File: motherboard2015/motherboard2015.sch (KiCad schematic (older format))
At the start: 29 parts, among them J1 RJ45, J2 RJ45, J3 RJ45, J4 RJ45, P1 DIL40

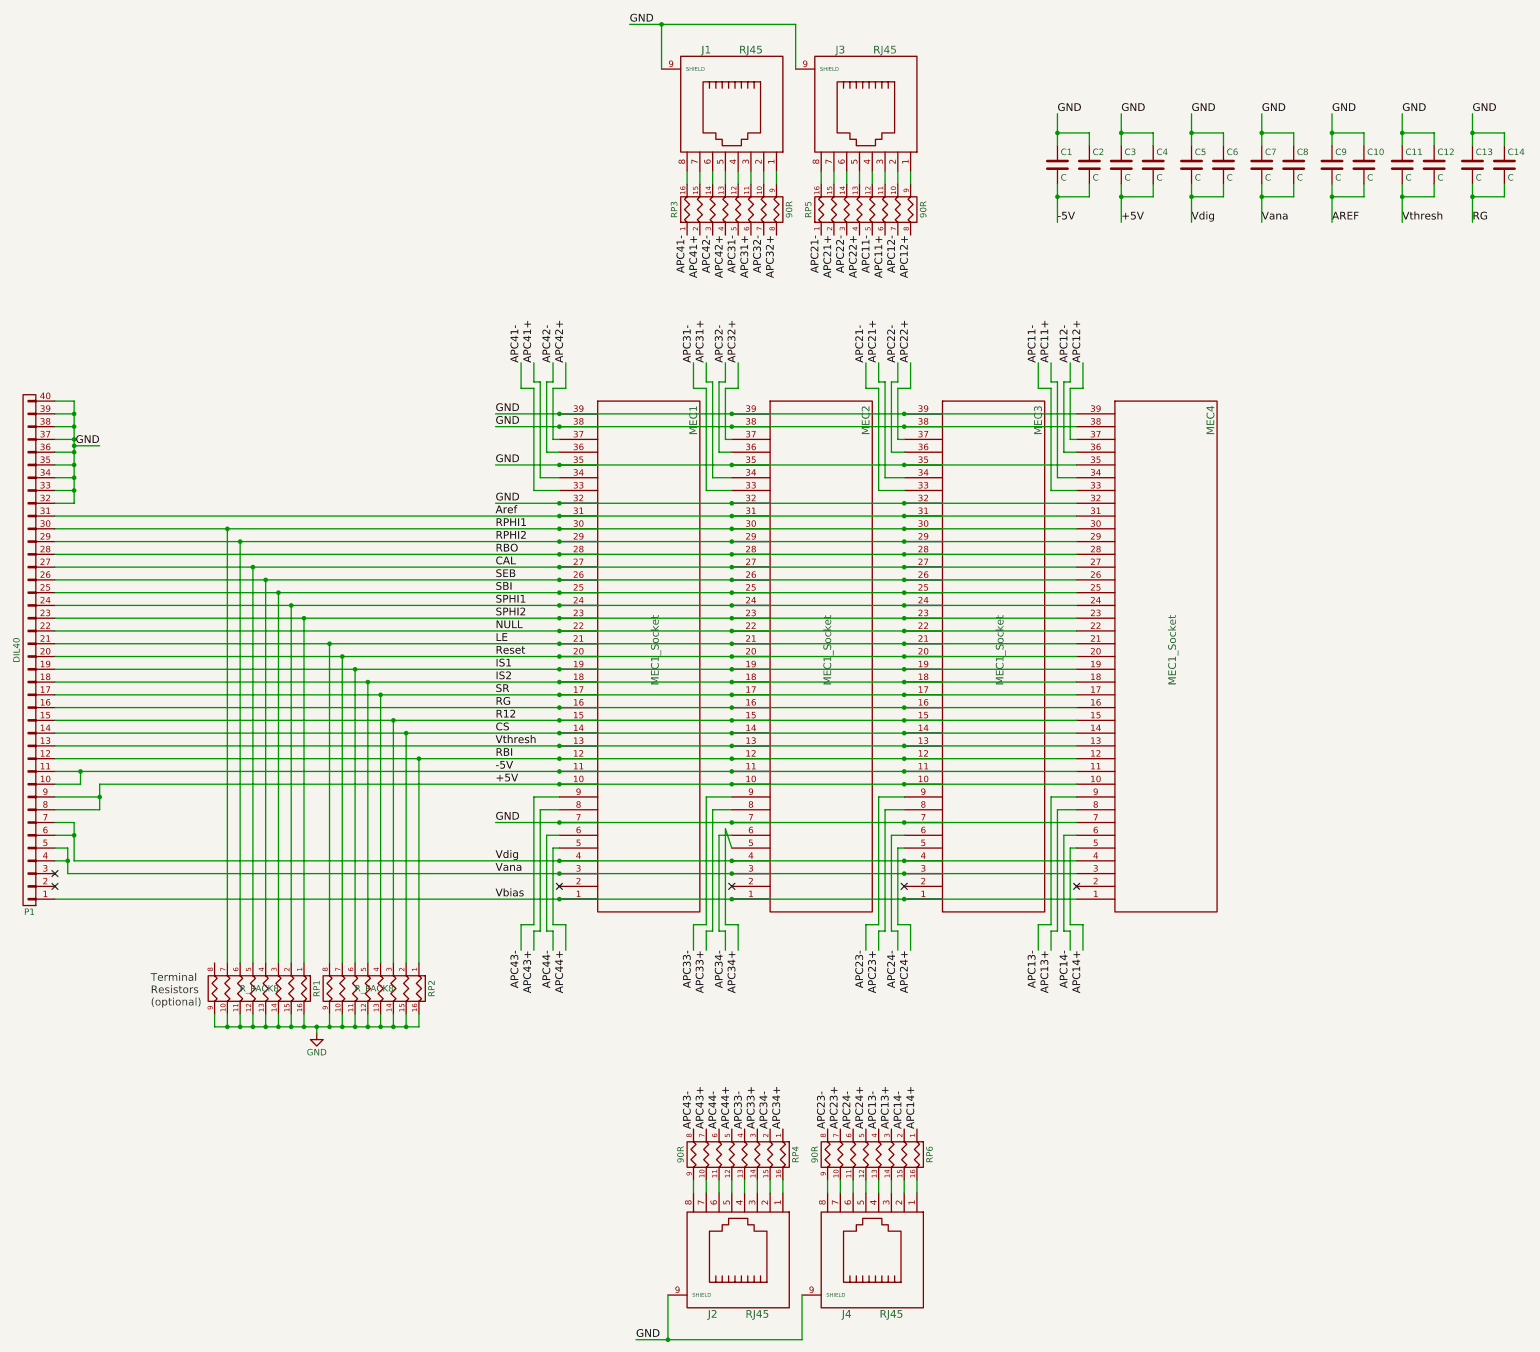
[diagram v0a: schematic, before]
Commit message: Updates to DAQ system including adjusting position of ZEM and adding Control signal outputs
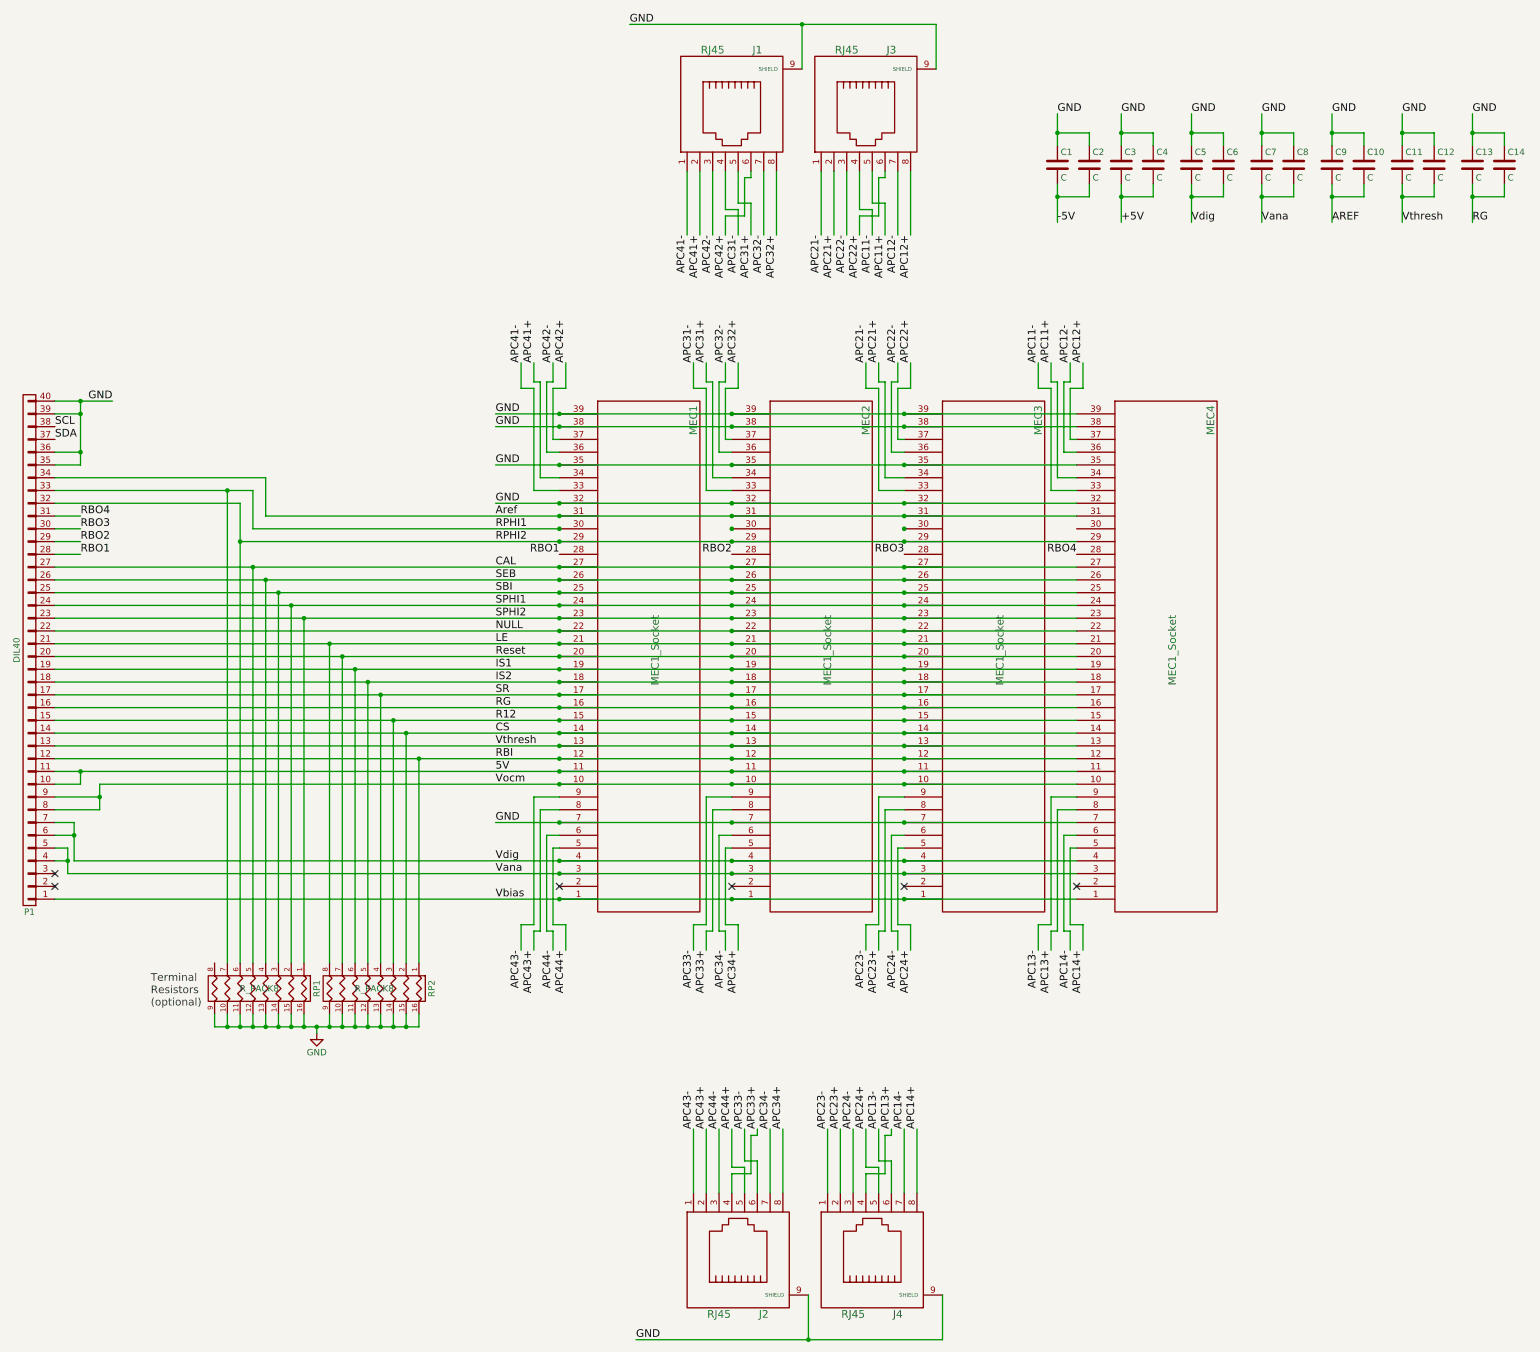
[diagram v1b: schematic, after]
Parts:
- removed RP3, RP4, RP5, RP6: 90R, extras:R8_MNR18, symbol R_PACK8
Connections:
- net +5V: no longer MEC1.10 (P10), MEC2.10 (P10), MEC3.10 (P10), MEC4.10 (P10), P1.8 (P8), P1.9 (P9)
- net -5V: no longer MEC1.11 (P11), MEC2.11 (P11), MEC3.11 (P11), MEC4.11 (P11), P1.10 (P10), P1.11 (P11)
- net APC11+: now also J3.5
- net APC11-: now also J3.4
- net APC12+: now also J3.8
- net APC12-: now also J3.7
- net APC13+: now also J4.4
- net APC13-: now also J4.6
- net APC14+: now also J4.8
- net APC14-: now also J4.7
- net APC21+: now also J3.2
- net APC21-: now also J3.1
- net APC22+: now also J3.6
- net APC22-: now also J3.3
- net APC23+: now also J4.2
- net APC23-: now also J4.1
- net APC24+: now also J4.5
- net APC24-: now also J4.3
- net APC31+: now also J1.5
- net APC31-: now also J1.4
- net APC32+: now also J1.8
- net APC32-: now also J1.7
- net APC33+: now also J2.4
- net APC33-: now also J2.6
- net APC34+: now also J2.8
- net APC34-: now also J2.7
- net APC41+: now also J1.2
- net APC41-: now also J1.1
- net APC42+: now also J1.6
- net APC42-: now also J1.3
- net APC43+: now also J2.2
- net APC43-: now also J2.1
- net APC44+: now also J2.5
- net APC44-: now also J2.3
- net Aref: now also P1.34 (P34); no longer P1.31 (P31)
- net GND: no longer P1.32 (P32), P1.33 (P33), P1.34 (P34), P1.37 (P37), P1.38 (P38)
- net RPHI1: now also P1.33 (P33); no longer MEC2.30 (P30), MEC3.30 (P30), MEC4.30 (P30), P1.30 (P30)
- net RPHI2: now also P1.32 (P32); no longer P1.29 (P29)
- removed net RBO: MEC1.28 (P28), MEC2.28 (P28), MEC3.28 (P28), MEC4.28 (P28), P1.28 (P28)
- new net 5V: MEC1.11 (P11), MEC2.11 (P11), MEC3.11 (P11), MEC4.11 (P11), P1.10 (P10), P1.11 (P11)
- new net RBO1: MEC1.28 (P28), P1.28 (P28)
- new net RBO2: MEC2.28 (P28), P1.29 (P29)
- new net RBO3: MEC3.28 (P28), P1.30 (P30)
- new net RBO4: MEC4.28 (P28), P1.31 (P31)
- new net SCL: P1.38 (P38)
- new net SDA: P1.37 (P37)
- new net Vocm: MEC1.10 (P10), MEC2.10 (P10), MEC3.10 (P10), MEC4.10 (P10), P1.8 (P8), P1.9 (P9)
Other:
- moved on the sheet: J1, J2, J3, J4

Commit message: bunch of updates
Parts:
- MEC1, MEC2, MEC3, MEC4: digipart (none) -> SAM8119-ND
- P1: footprint Pin_Headers:Pin_Header_Straight_2x20 -> extras:Pin_Header_Straight_2x20
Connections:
- net APC33+: now also J2.5; no longer J2.4
- net APC33-: now also J2.3; no longer J2.6
- net APC34+: now also J2.2; no longer J2.8
- net APC34-: now also J2.1; no longer J2.7
- net APC43+: now also J2.8; no longer J2.2
- net APC43-: now also J2.7; no longer J2.1
- net APC44+: now also J2.4; no longer J2.5
- net APC44-: now also J2.6; no longer J2.3

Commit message: Additional work on motherboard, removes some extraneous files
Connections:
- net APC13+: now also J4.5; no longer J4.4
- net APC13-: now also J4.3; no longer J4.6
- net APC14+: now also J4.2; no longer J4.8
- net APC14-: now also J4.1; no longer J4.7
- net APC23+: now also J4.8; no longer J4.2
- net APC23-: now also J4.7; no longer J4.1
- net APC24+: now also J4.4; no longer J4.5
- net APC24-: now also J4.6; no longer J4.3
- net CAL: now also RP1.12 (R5); no longer RP1.5 (P5)
- net CS: now also RP2.15 (R2); no longer RP2.2 (P2)
- net GND: now also RP1.1 (P1), RP1.2 (P2), RP1.3 (P3), RP1.4 (P4), RP1.5 (P5), RP1.6 (P6), RP1.7 (P7), RP1.8 (P8), RP2.1 (P1), RP2.2 (P2), RP2.3 (P3), RP2.4 (P4), RP2.5 (P5), RP2.6 (P6), RP2.7 (P7), RP2.8 (P8); no longer RP1.10 (R7), RP1.11 (R6), RP1.12 (R5), RP1.13 (R4), RP1.14 (R3), RP1.15 (R2), RP1.16 (R1), RP1.9 (R8), RP2.10 (R7), RP2.11 (R6), RP2.12 (R5), RP2.13 (R4), RP2.14 (R3), RP2.15 (R2), RP2.16 (R1), RP2.9 (R8)
- net IS1: now also RP2.11 (R6); no longer RP2.6 (P6)
- net IS2: now also RP2.12 (R5); no longer RP2.5 (P5)
- net LE: now also RP2.9 (R8); no longer RP2.8 (P8)
- net R12: now also RP2.14 (R3); no longer RP2.3 (P3)
- net RBI: now also RP2.16 (R1); no longer RP2.1 (P1)
- net RPHI1: now also RP1.10 (R7); no longer RP1.7 (P7)
- net RPHI2: now also RP1.11 (R6); no longer RP1.6 (P6)
- net Reset: now also RP2.10 (R7); no longer RP2.7 (P7)
- net SBI: now also RP1.14 (R3); no longer RP1.3 (P3)
- net SEB: now also RP1.13 (R4); no longer RP1.4 (P4)
- net SPHI1: now also RP1.15 (R2); no longer RP1.2 (P2)
- net SPHI2: now also RP1.16 (R1); no longer RP1.1 (P1)
- net SR: now also RP2.13 (R4); no longer RP2.4 (P4)
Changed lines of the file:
@@
 Text Label 7400 11000 0    60   ~ 0
 GND
+Text Label 9000 9350 1    60   ~ 0
+APC14+
+Text Label 8900 9350 1    60   ~ 0
+APC14-
+Text Label 9200 9350 1    60   ~ 0
+APC13+
+Text Label 9100 9350 1    60   ~ 0
+APC13-
+Text Label 9400 9350 1    60   ~ 0
+APC24+
+Text Label 9300 9350 1    60   ~ 0
+APC24-
 Text Label 9600 9350 1    60   ~ 0
-APC14+
+APC23+
 Text Label 9500 9350 1    60   ~ 0
-APC14-
-Text Label 9400 9350 1    60   ~ 0
-APC13+
-Text Label 9300 9350 1    60   ~ 0
-APC13-
-Text Label 9200 9350 1    60   ~ 0
-APC24+
-Text Label 9100 9350 1    60   ~ 0
-APC24-
-Text Label 9000 9350 1    60   ~ 0
-APC23+
-Text Label 8900 9350 1    60   ~ 0
 APC23-
 Text Label 7950 9350 1    60   ~ 0
@@
 F 3 "" H 5350 8250 60  0000 C CNN
 	1    5350 8250
-	0    1    1    0
+	0    1    -1   0
 $EndComp
 $Comp
@@
 F 3 "" H 4450 8250 60  0000 C CNN
 	1    4450 8250
-	0    1    1    0
+	0    1    -1   0
 $EndComp
 $Comp
@@
 	6800 4650 4400 4650
 Wire Wire Line
-	4400 4350 4400 4650
-Wire Wire Line
-	2850 4350 4400 4350
+	4400 4650 4400 4350
+Wire Wire Line
+	4400 4350 2850 4350
 Wire Wire Line
 	4300 4450 2850 4450

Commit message: annotates parts for new build-management tool
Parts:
- C1, C10, C11, C12, C13, C14, C2, C3, C4, C5, C6, C7, C8, C9: footprint SMD_Packages:SMD-0603 -> Capacitors_SMD:C_0603
- MEC1, MEC2, MEC3, MEC4: Digikey (none) -> SAM8119-ND; digipart SAM8119-ND -> (none)
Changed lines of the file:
@@
 F 0 "C9" H 12875 1900 50  0000 L CNN
 F 1 "C" H 12875 1700 50  0000 L CNN
-F 2 "SMD_Packages:SMD-0603" H 12888 1650 30  0001 C CNN
+F 2 "Capacitors_SMD:C_0603" H 12888 1650 30  0001 C CNN
 F 3 "" H 12850 1800 60  0000 C CNN
 	1    12850 1800
@@
 F 0 "C11" H 13425 1900 50  0000 L CNN
 F 1 "C" H 13425 1700 50  0000 L CNN
-F 2 "SMD_Packages:SMD-0603" H 13438 1650 30  0001 C CNN
+F 2 "Capacitors_SMD:C_0603" H 13438 1650 30  0001 C CNN
 F 3 "" H 13400 1800 60  0000 C CNN
 	1    13400 1800
@@
 F 0 "C13" H 13975 1900 50  0000 L CNN
 F 1 "C" H 13975 1700 50  0000 L CNN
-F 2 "SMD_Packages:SMD-0603" H 13988 1650 30  0001 C CNN
+F 2 "Capacitors_SMD:C_0603" H 13988 1650 30  0001 C CNN
 F 3 "" H 13950 1800 60  0000 C CNN
 	1    13950 1800
@@
 F 2 "extras:MEC1" H 7550 5600 60  0001 C CNN
 F 3 "" H 7550 5600 60  0000 C CNN
-F 4 "SAM8119-ND" H 7550 5600 60  0001 C CNN "digipart"
+F 4 "SAM8119-ND" H 7550 5600 60  0001 C CNN "Digikey"
 	1    7550 5600
 	0    -1   -1   0
@@
 F 2 "extras:MEC1" H 8900 5600 60  0001 C CNN
 F 3 "" H 8900 5600 60  0000 C CNN
-F 4 "SAM8119-ND" H 8900 5600 60  0001 C CNN "digipart"
+F 4 "SAM8119-ND" H 8900 5600 60  0001 C CNN "Digikey"
 	1    8900 5600
 	0    -1   -1   0
@@
 F 2 "extras:MEC1" H 10250 5600 60  0001 C CNN
 F 3 "" H 10250 5600 60  0000 C CNN
-F 4 "SAM8119-ND" H 10250 5600 60  0001 C CNN "digipart"
+F 4 "SAM8119-ND" H 10250 5600 60  0001 C CNN "Digikey"
 	1    10250 5600
 	0    -1   -1   0
@@
 F 2 "extras:MEC1" H 11600 5600 60  0001 C CNN
 F 3 "" H 11600 5600 60  0000 C CNN
-F 4 " SAM8119-ND" H 11600 5600 60  0001 C CNN "digipart"
+F 4 "SAM8119-ND" H 11600 5600 60  0001 C CNN "Digikey"
 	1    11600 5600
 	0    -1   -1   0
@@
 F 0 "C14" H 14225 1900 50  0000 L CNN
 F 1 "C" H 14225 1700 50  0000 L CNN
-F 2 "SMD_Packages:SMD-0603" H 14238 1650 30  0001 C CNN
+F 2 "Capacitors_SMD:C_0603" H 14238 1650 30  0001 C CNN
 F 3 "" H 14200 1800 60  0000 C CNN
 	1    14200 1800
@@
 F 0 "C12" H 13675 1900 50  0000 L CNN
 F 1 "C" H 13675 1700 50  0000 L CNN
-F 2 "SMD_Packages:SMD-0603" H 13688 1650 30  0001 C CNN
+F 2 "Capacitors_SMD:C_0603" H 13688 1650 30  0001 C CNN
 F 3 "" H 13650 1800 60  0000 C CNN
 	1    13650 1800
@@
 F 0 "C10" H 13125 1900 50  0000 L CNN
 F 1 "C" H 13125 1700 50  0000 L CNN
-F 2 "SMD_Packages:SMD-0603" H 13138 1650 30  0001 C CNN
+F 2 "Capacitors_SMD:C_0603" H 13138 1650 30  0001 C CNN
 F 3 "" H 13100 1800 60  0000 C CNN
 	1    13100 1800
@@
 F 0 "C7" H 12325 1900 50  0000 L CNN
 F 1 "C" H 12325 1700 50  0000 L CNN
-F 2 "SMD_Packages:SMD-0603" H 12338 1650 30  0001 C CNN
+F 2 "Capacitors_SMD:C_0603" H 12338 1650 30  0001 C CNN
 F 3 "" H 12300 1800 60  0000 C CNN
 	1    12300 1800
@@
 F 0 "C8" H 12575 1900 50  0000 L CNN
 F 1 "C" H 12575 1700 50  0000 L CNN
-F 2 "SMD_Packages:SMD-0603" H 12588 1650 30  0001 C CNN
+F 2 "Capacitors_SMD:C_0603" H 12588 1650 30  0001 C CNN
 F 3 "" H 12550 1800 60  0000 C CNN
 	1    12550 1800
@@
 F 0 "C5" H 11775 1900 50  0000 L CNN
 F 1 "C" H 11775 1700 50  0000 L CNN
-F 2 "SMD_Packages:SMD-0603" H 11788 1650 30  0001 C CNN
+F 2 "Capacitors_SMD:C_0603" H 11788 1650 30  0001 C CNN
 F 3 "" H 11750 1800 60  0000 C CNN
 	1    11750 1800
@@
 F 0 "C6" H 12025 1900 50  0000 L CNN
 F 1 "C" H 12025 1700 50  0000 L CNN
-F 2 "SMD_Packages:SMD-0603" H 12038 1650 30  0001 C CNN
+F 2 "Capacitors_SMD:C_0603" H 12038 1650 30  0001 C CNN
 F 3 "" H 12000 1800 60  0000 C CNN
 	1    12000 1800
@@
 F 0 "C3" H 11225 1900 50  0000 L CNN
 F 1 "C" H 11225 1700 50  0000 L CNN
-F 2 "SMD_Packages:SMD-0603" H 11238 1650 30  0001 C CNN
+F 2 "Capacitors_SMD:C_0603" H 11238 1650 30  0001 C CNN
 F 3 "" H 11200 1800 60  0000 C CNN
 	1    11200 1800
@@
 F 0 "C4" H 11475 1900 50  0000 L CNN
 F 1 "C" H 11475 1700 50  0000 L CNN
-F 2 "SMD_Packages:SMD-0603" H 11488 1650 30  0001 C CNN
+F 2 "Capacitors_SMD:C_0603" H 11488 1650 30  0001 C CNN
 F 3 "" H 11450 1800 60  0000 C CNN
 	1    11450 1800
@@
 F 0 "C1" H 10725 1900 50  0000 L CNN
 F 1 "C" H 10725 1700 50  0000 L CNN
-F 2 "SMD_Packages:SMD-0603" H 10738 1650 30  0001 C CNN
+F 2 "Capacitors_SMD:C_0603" H 10738 1650 30  0001 C CNN
 F 3 "" H 10700 1800 60  0000 C CNN
 	1    10700 1800
@@
 F 0 "C2" H 10975 1900 50  0000 L CNN
 F 1 "C" H 10975 1700 50  0000 L CNN
-F 2 "SMD_Packages:SMD-0603" H 10988 1650 30  0001 C CNN
+F 2 "Capacitors_SMD:C_0603" H 10988 1650 30  0001 C CNN
 F 3 "" H 10950 1800 60  0000 C CNN
 	1    10950 1800
